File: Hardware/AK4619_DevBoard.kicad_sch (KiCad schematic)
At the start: 78 parts, among them J1 Power, J2 Power, J3 In, J4 Out, J5 Out_Amp, J6 Conn_02x08_Odd_Even, J7 Conn_02x15_Odd_Even, J8 Conn_02x10_Odd_Even, J9 Conn_02x17_Odd_Even, U1 TL074, U2 MCP6004, U3 Hyperram_BGA, U4 AK4619VN

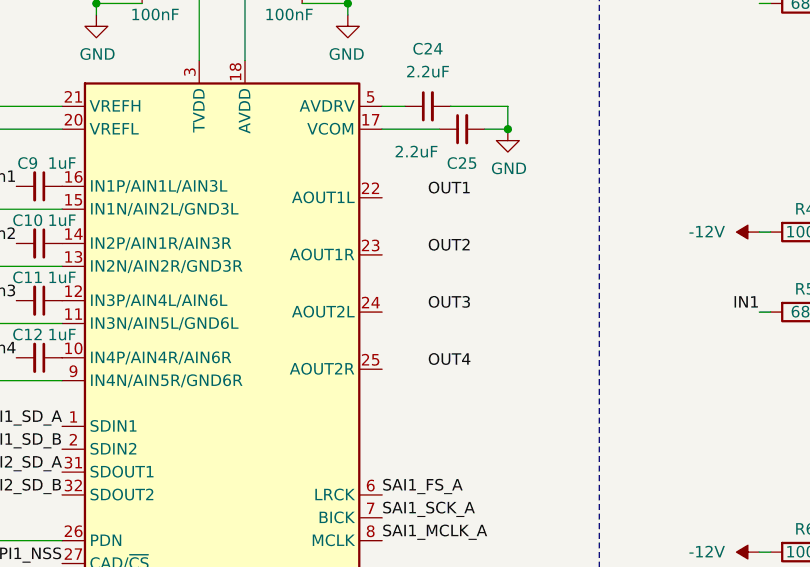
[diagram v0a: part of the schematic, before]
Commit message: Clocked delay working; fixes to flanger
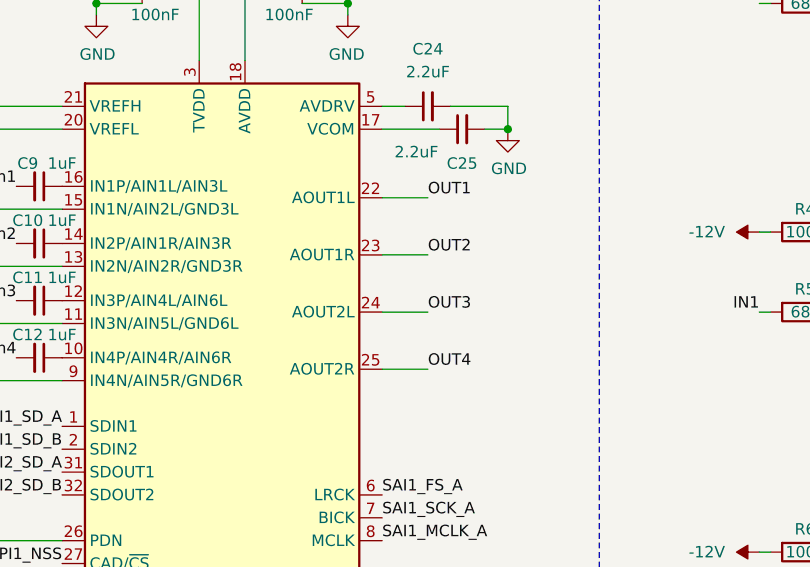
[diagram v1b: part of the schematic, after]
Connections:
- net OUT1: now also U4.22 (AOUT1L)
- net OUT2: now also U4.23 (AOUT1R)
- net OUT3: now also U4.24 (AOUT2L)
- net OUT4: now also U4.25 (AOUT2R)
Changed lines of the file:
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@@
+    (stroke (width 0) (type default))
+  )
+  (wire (pts (xy 186.69 58.42) (xy 191.77 58.42))
     (stroke (width 0) (type default))
   )
@@
     (stroke (width 0) (type default))
   )
+  (wire (pts (xy 186.69 71.12) (xy 191.77 71.12))
+    (stroke (width 0) (type default))
+  )
   (wire (pts (xy 300.99 33.02) (xy 300.99 34.29))
     (stroke (width 0) (type default))
@@
     (stroke (width 0) (type default))
   )
+  (wire (pts (xy 186.69 52.07) (xy 191.77 52.07))
+    (stroke (width 0) (type default))
+  )
   (wire (pts (xy 299.72 100.33) (xy 299.72 101.6))
     (stroke (width 0) (type default))
@@
     (stroke (width 0) (type default))
   )
+  (wire (pts (xy 186.69 64.77) (xy 191.77 64.77))
+    (stroke (width 0) (type default))
+  )
